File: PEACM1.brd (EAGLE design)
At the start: 160 x 100 mm, 15 parts

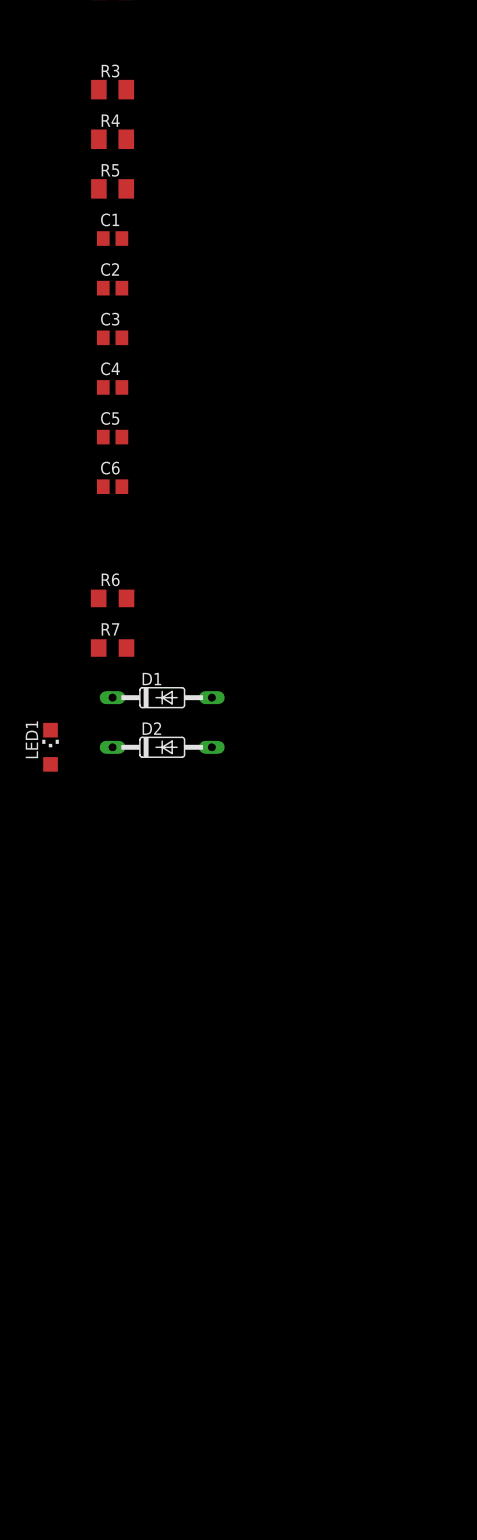
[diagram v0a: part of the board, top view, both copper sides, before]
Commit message: Schematic components from example complete. Needs connectors, V+ for OpAmp.
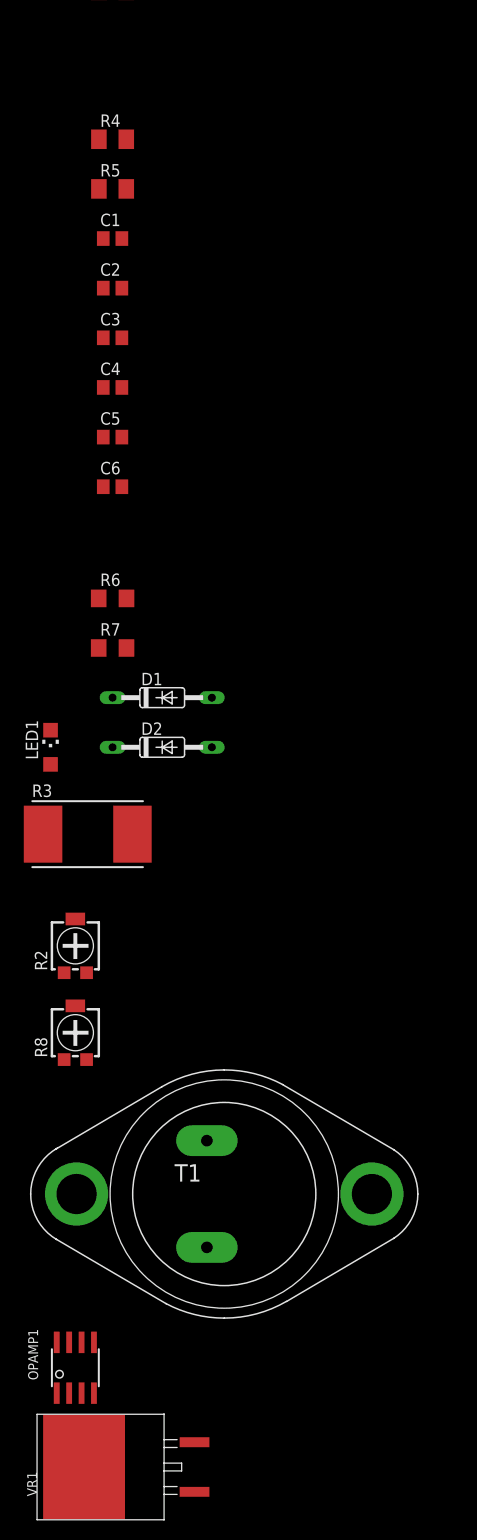
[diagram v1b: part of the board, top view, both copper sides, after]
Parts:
- added OPAMP1: LM301AD, PEAC:SOIC8
- added R2, R8: (no value), rcl:RTRIM4G/J
- added T1: MJ4502, transistor:TO3
- added VR1: LM317, PEAC:D2PAK-3
- R1: value (none) -> 33
- R3: value (none) -> 0.2 5W; device rcl:M1206 -> rcl:R4527
- R4: value (none) -> 680
- R5: value (none) -> 330k
- R6: value (none) -> 240
- moved R3 76.2 mm to (0.00, -90.2)
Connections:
- new net +1.2-30V: C3.1, D2.C, OPAMP1.3, R3.1, R4.2, R6.2, VR1.VOUT
- new net N$1: C4.2, OPAMP1.1
- new net VCC+@7: OPAMP1.7
- new net VCC-@4: OPAMP1.4
- net +35V: now also T1.E
- net GND: now also R8.2
- net N$11: now also OPAMP1.6
- net N$2: now also R2.3, T1.C
- net N$3: now also R1.2, T1.B, VR1.VIN; no longer C3.1, D2.C, R3.1, R4.2, R6.2
- net N$4: now also OPAMP1.2, R2.2
- net N$5: now also VR1.ADJ
- net N$6: now also R8.3
- net N$9: now also OPAMP1.8
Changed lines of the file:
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@@
 </autorouter>
 <elements>
-<element name="R1" library="rcl" package="M1206" value="" x="2.54" y="-3.81"/>
-<element name="R3" library="rcl" package="M1206" value="" x="2.54" y="-13.97"/>
-<element name="R4" library="rcl" package="M1206" value="" x="2.54" y="-19.05"/>
-<element name="R5" library="rcl" package="M1206" value="" x="2.54" y="-24.13"/>
+<element name="R1" library="rcl" package="M1206" value="33" x="2.54" y="-3.81"/>
+<element name="R4" library="rcl" package="M1206" value="680" x="2.54" y="-19.05"/>
+<element name="R5" library="rcl" package="M1206" value="330k" x="2.54" y="-24.13"/>
 <element name="C1" library="rcl" package="C0805" value="1u" x="2.54" y="-29.21"/>
 <element name="C2" library="rcl" package="C0805" value="100p" x="2.54" y="-34.29"/>
@@
 <element name="C5" library="rcl" package="C0805" value="75p" x="2.54" y="-49.53"/>
 <element name="C6" library="rcl" package="C0805" value="10u" x="2.54" y="-54.61"/>
-<element name="R6" library="rcl" package="R1206" value="" x="2.54" y="-66.04"/>
+<element name="R6" library="rcl" package="R1206" value="240" x="2.54" y="-66.04"/>
 <element name="R7" library="rcl" package="R1206" value="" x="2.54" y="-71.12"/>
 <element name="D1" library="diode" package="DO35-10" value="1N457" x="7.62" y="-76.2"/>
 <element name="D2" library="diode" package="DO35-10" value="1N457" x="7.62" y="-81.28"/>
 <element name="LED1" library="led" package="CHIPLED_1206" value="" x="-3.81" y="-81.28"/>
+<element name="R3" library="rcl" package="R4527" value="0.2 5W" x="0" y="-90.17"/>
+<element name="R2" library="rcl" package="RTRIM4G/J" value="" x="-1.27" y="-101.6"/>
+<element name="R8" library="rcl" package="RTRIM4G/J" value="" x="-1.27" y="-110.49"/>
+<element name="T1" library="transistor" package="TO3" value="MJ4502" x="13.97" y="-127"/>
+<element name="OPAMP1" library="PEAC" package="SOIC8" value="LM301AD" x="-1.27" y="-144.78"/>
+<element name="VR1" library="PEAC" package="D2PAK-3" value="LM317" x="3.81" y="-154.94"/>
 </elements>
 <signals>
@@
 <contactref element="C6" pad="2"/>
 <contactref element="C3" pad="2"/>
+<contactref element="R8" pad="2"/>
+<wire x1="3.49" y1="-54.61" x2="-1.27" y2="-107.74" width="0" layer="19" extent="1-1"/>
 <wire x1="3.49" y1="-39.37" x2="3.49" y2="-54.61" width="0" layer="19" extent="1-1"/>
 <wire x1="3.49" y1="-29.21" x2="3.49" y2="-39.37" width="0" layer="19" extent="1-1"/>
 </signal>
 <signal name="N$2">
+<contactref element="C2" pad="1"/>
 <contactref element="R3" pad="2"/>
-<contactref element="C2" pad="1"/>
-<wire x1="3.94" y1="-13.97" x2="1.59" y2="-34.29" width="0" layer="19" extent="1-1"/>
-</signal>
-<signal name="N$3">
-<contactref element="C3" pad="1"/>
-<contactref element="R3" pad="1"/>
-<contactref element="R4" pad="2"/>
-<contactref element="R6" pad="2"/>
-<contactref element="D2" pad="C"/>
-<wire x1="3.962" y1="-66.04" x2="2.54" y2="-81.28" width="0" layer="19" extent="1-1"/>
-<wire x1="1.59" y1="-39.37" x2="3.962" y2="-66.04" width="0" layer="19" extent="1-1"/>
-<wire x1="3.94" y1="-19.05" x2="1.59" y2="-39.37" width="0" layer="19" extent="1-1"/>
-<wire x1="1.14" y1="-13.97" x2="3.94" y2="-19.05" width="0" layer="19" extent="1-1"/>
+<contactref element="R2" pad="3"/>
+<contactref element="T1" pad="C"/>
+<wire x1="4.575" y1="-90.17" x2="-0.12" y2="-104.35" width="0" layer="19" extent="1-1"/>
+<wire x1="29.083" y1="-127" x2="-0.12" y2="-104.35" width="0" layer="19" extent="1-1"/>
+<wire x1="1.59" y1="-34.29" x2="4.575" y2="-90.17" width="0" layer="19" extent="1-1"/>
 </signal>
 <signal name="N$4">
@@
 <contactref element="R5" pad="2"/>
 <contactref element="C5" pad="2"/>
+<contactref element="R2" pad="2"/>
+<contactref element="OPAMP1" pad="2"/>
+<wire x1="-1.27" y1="-98.85" x2="-1.905" y2="-147.38" width="0" layer="19" extent="1-1"/>
+<wire x1="3.49" y1="-49.53" x2="-1.27" y2="-98.85" width="0" layer="19" extent="1-1"/>
 <wire x1="3.49" y1="-34.29" x2="3.49" y2="-49.53" width="0" layer="19" extent="1-1"/>
 <wire x1="3.94" y1="-24.13" x2="3.49" y2="-34.29" width="0" layer="19" extent="1-1"/>
@@
 <contactref element="R7" pad="2"/>
 <contactref element="D1" pad="A"/>
-<wire x1="12.7" y1="-76.2" x2="3.962" y2="-71.12" width="0" layer="19" extent="1-1"/>
+<contactref element="VR1" pad="ADJ"/>
+<wire x1="12.7" y1="-76.2" x2="10.93" y2="-157.48" width="0" layer="19" extent="1-1"/>
+<wire x1="3.962" y1="-71.12" x2="12.7" y2="-76.2" width="0" layer="19" extent="1-1"/>
 <wire x1="1.14" y1="-24.13" x2="3.962" y2="-71.12" width="0" layer="19" extent="1-1"/>
 </signal>
@@
 <contactref element="R6" pad="1"/>
 <contactref element="C6" pad="1"/>
+<contactref element="R8" pad="3"/>
+<wire x1="1.118" y1="-71.12" x2="-0.12" y2="-113.24" width="0" layer="19" extent="1-1"/>
 <wire x1="1.118" y1="-66.04" x2="1.118" y2="-71.12" width="0" layer="19" extent="1-1"/>
 <wire x1="1.59" y1="-54.61" x2="1.118" y2="-66.04" width="0" layer="19" extent="1-1"/>
@@
 <contactref element="D2" pad="A"/>
 <contactref element="C4" pad="1"/>
+<contactref element="OPAMP1" pad="8"/>
+<wire x1="12.7" y1="-81.28" x2="-3.175" y2="-142.18" width="0" layer="19" extent="1-1"/>
 <wire x1="1.59" y1="-44.45" x2="12.7" y2="-81.28" width="0" layer="19" extent="1-1"/>
 </signal>
@@
 <contactref element="LED1" pad="C"/>
 <contactref element="C5" pad="1"/>
+<contactref element="OPAMP1" pad="6"/>
+<wire x1="-3.81" y1="-79.53" x2="-0.635" y2="-142.18" width="0" layer="19" extent="1-1"/>
 <wire x1="1.59" y1="-49.53" x2="-3.81" y2="-79.53" width="0" layer="19" extent="1-1"/>
 </signal>
@@
 <contactref element="C1" pad="1"/>
 <contactref element="R1" pad="1"/>
+<contactref element="T1" pad="E"/>
+<wire x1="1.59" y1="-29.21" x2="12.192" y2="-132.461" width="0" layer="19" extent="1-1"/>
 <wire x1="1.14" y1="-3.81" x2="1.59" y2="-29.21" width="0" layer="19" extent="1-1"/>
 </signal>
+<signal name="+1.2-30V">
+<contactref element="C3" pad="1"/>
+<contactref element="R4" pad="2"/>
+<contactref element="R6" pad="2"/>
+<contactref element="D2" pad="C"/>
+<contactref element="R3" pad="1"/>
+<contactref element="OPAMP1" pad="3"/>
+<contactref element="VR1" pad="VOUT"/>
+<wire x1="-0.635" y1="-147.38" x2="-0.38" y2="-154.94" width="0" layer="19" extent="1-1"/>
+<wire x1="-4.575" y1="-90.17" x2="-0.635" y2="-147.38" width="0" layer="19" extent="1-1"/>
+<wire x1="2.54" y1="-81.28" x2="-4.575" y2="-90.17" width="0" layer="19" extent="1-1"/>
+<wire x1="3.962" y1="-66.04" x2="2.54" y2="-81.28" width="0" layer="19" extent="1-1"/>
+<wire x1="1.59" y1="-39.37" x2="3.962" y2="-66.04" width="0" layer="19" extent="1-1"/>
+<wire x1="3.94" y1="-19.05" x2="1.59" y2="-39.37" width="0" layer="19" extent="1-1"/>
+</signal>
+<signal name="N$3">
+<contactref element="T1" pad="B"/>
+<contactref element="R1" pad="2"/>
+<contactref element="VR1" pad="VIN"/>
+<wire x1="12.192" y1="-121.539" x2="10.93" y2="-152.4" width="0" layer="19" extent="1-1"/>
+<wire x1="3.94" y1="-3.81" x2="12.192" y2="-121.539" width="0" layer="19" extent="1-1"/>
+</signal>
+<signal name="N$1">
+<contactref element="OPAMP1" pad="1"/>
+<contactref element="C4" pad="2"/>
+<wire x1="3.49" y1="-44.45" x2="-3.175" y2="-147.38" width="0" layer="19" extent="1-1"/>
+</signal>
+<signal name="VCC+@7">
+<contactref element="OPAMP1" pad="7"/>
+</signal>
+<signal name="VCC-@4">
+<contactref element="OPAMP1" pad="4"/>
+</signal>
 </signals>

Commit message: Schematic and layout ready for review.
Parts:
- added H1, H2: MOUNT-PAD-ROUND2.8, holes:2,8-PAD
- added JP1, JP2: (no value), pinhead:1X02
- added R9: NU, rcl:M1206
- R7: value (none) -> 220
- moved VR1 188.0 mm to (52.6, 26.7), turned to 90 degrees
- moved OPAMP1 187.7 mm to (82.5, 23.1)
- moved R8 159.0 mm to (43.2, 42.2), turned to 90 degrees
- moved R2 146.9 mm to (28.7, 42.2), turned to 270 degrees
- moved T1 143.6 mm to (23.9, 16.3), turned to 180 degrees
- moved LED1 137.3 mm to (74.2, 31.8), turned to 270 degrees
- moved D1 128.6 mm to (66.5, 38.1), turned to 180 degrees
- moved R7 120.1 mm to (61.5, 33.5), turned to 90 degrees
- moved D2 117.5 mm to (66.5, 20.3)
- moved R3 110.9 mm to (51.8, 7.87), turned to 180 degrees
- moved R6 110.1 mm to (61.5, 26.9), turned to 270 degrees
- moved C6 106.8 mm to (67.1, 30.5)
- moved C5 106.7 mm to (76.7, 27.2), turned to 270 degrees
- moved C4 97.9 mm to (76.5, 19.8), turned to 270 degrees
- moved C3 92.9 mm to (78.2, 14.5), turned to 270 degrees
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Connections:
- removed net VCC+@7: OPAMP1.7
- removed net VCC-@4: OPAMP1.4
- new net VCC-: OPAMP1.4, R9.2
- net +1.2-30V: now also JP2.1
- net +35V: now also JP1.2, OPAMP1.7
- net GND: now also H1.B2,8, H2.B2,8, JP1.1, JP2.2, R9.1
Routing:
- net +35V: track 0.00 -> 112.4 mm, vias 0 -> 1
- net N$2: track 0.00 -> 91.9 mm
- net +1.2-30V: track 0.00 -> 77.3 mm
- net N$4: track 0.00 -> 64.1 mm, vias 0 -> 5
- net N$3: track 0.00 -> 40.7 mm
- net N$6: track 0.00 -> 34.4 mm
- net N$5: track 0.00 -> 14.7 mm
- net N$8: track 0.00 -> 13.3 mm
- net N$9: track 0.00 -> 12.6 mm
- net N$11: track 0.00 -> 12.5 mm
- net VCC-: track 0.00 -> 10.8 mm
- net N$1: track 0.00 -> 5.51 mm
- net GND: track 0.00 -> 0.18 mm, vias 0 -> 36
- added copper zone on layer 1, net GND
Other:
- board size 160 x 100 mm -> 91.7 x 48.7 mm
- board text added: "1.2-30V Current/ Voltage Regulator"
- board text added: "PEAC"
- board text added: "Rob Gaskell"

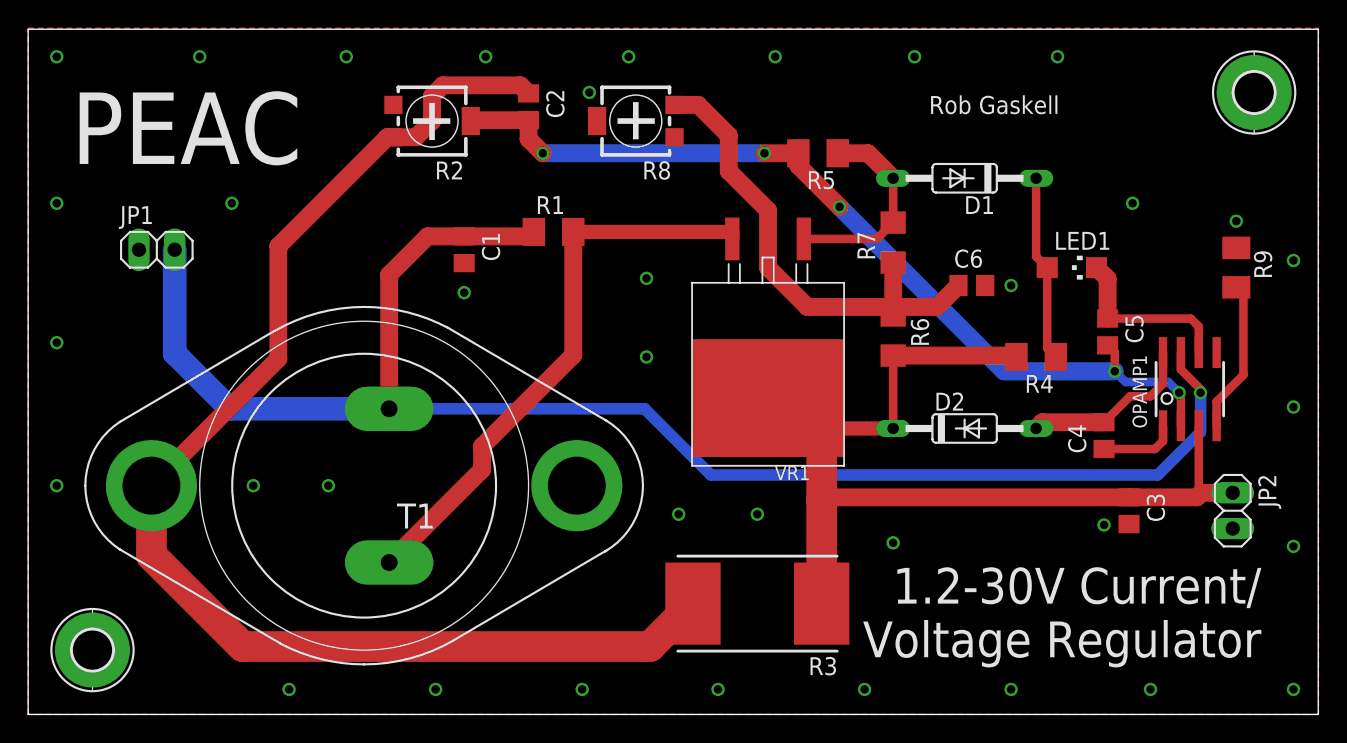
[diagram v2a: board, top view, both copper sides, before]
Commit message: Completed board layout.
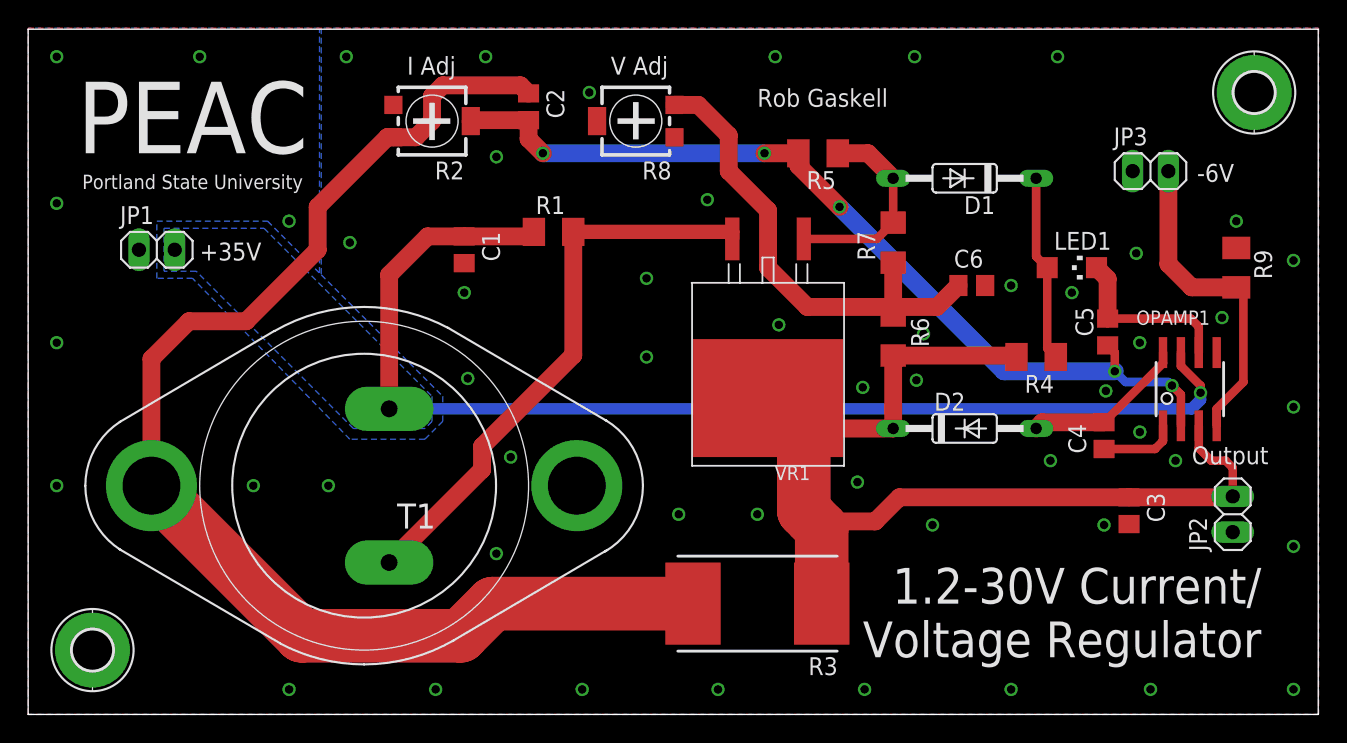
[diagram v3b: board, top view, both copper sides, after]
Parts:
- added JP3: (no value), pinhead:1X02
- moved JP2 0.25 mm to (85.6, 14.2)
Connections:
- net GND: now also JP3.1
- net VCC-: now also JP3.2
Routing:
- net +35V: track 112.4 -> 82.9 mm
- net VCC-: track 10.8 -> 23.0 mm
- net +1.2-30V: track 77.3 -> 74.3 mm
- net N$2: track 91.9 -> 90.8 mm
- net N$9: track 12.6 -> 11.7 mm
- net GND: vias 36 -> 53
- added copper zone on layer 16, net +35V
- added copper zone on layer 16, net GND
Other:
- board text added: "+35V"
- board text added: "-6V"
- board text added: "I Adj"
- board text added: "Output"
- board text added: "Portland State University"
- board text added: "V Adj"
